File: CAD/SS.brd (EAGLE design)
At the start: 77 x 109 mm, 82 parts, among them Q1 SN74AHC-OR, Q2 UMD5N, Q4 SN74AHC-OR, Q5 BFP460, Q6 L78L05, Q7 NCP553, T1 MMBTRA104SS

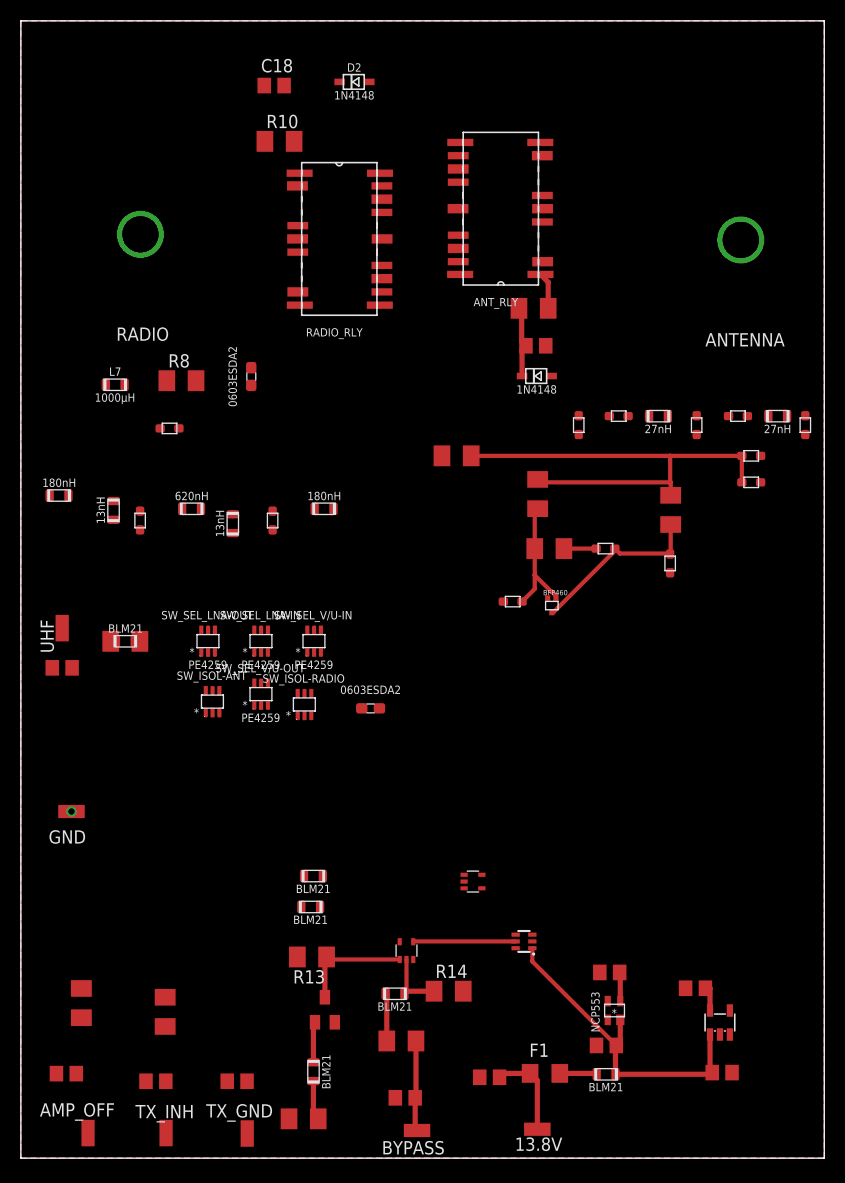
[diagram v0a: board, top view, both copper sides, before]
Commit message: Board: Pouring some copper over it
Started designing the board layout.
Plus, schematic: Fixed an error on 100R relay resistor placement
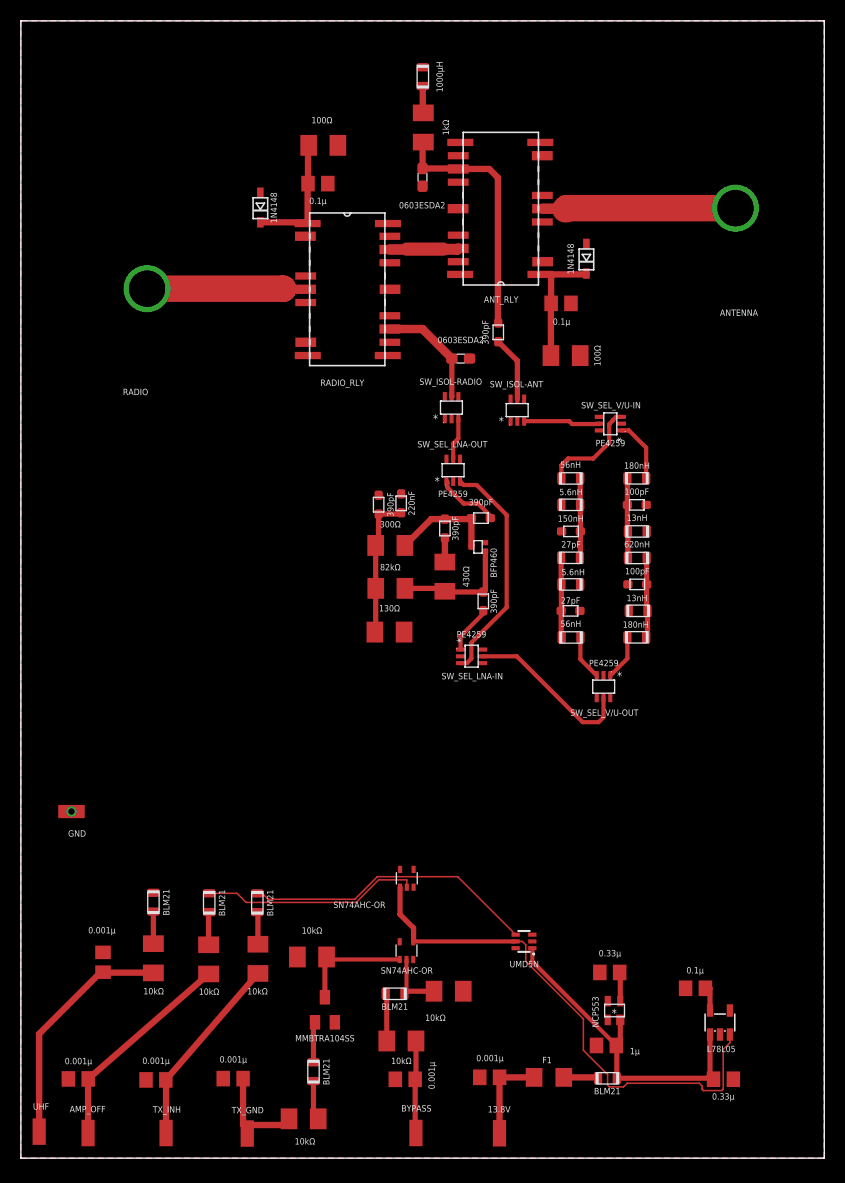
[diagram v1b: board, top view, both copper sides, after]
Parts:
- removed C3: 27pF, aarf:GRM18
- removed C4, C5: 6.8pF, aarf:GRM18
- added L10, L11: 5.6nH, aarf:0805
- added L9: 56nH, aarf:0805
- C6: value 43pF -> 27pF
- C7: value 4.7pF -> 27pF
- L6: value 27nH -> 56nH
- L8: value 27nH -> 150nH
- moved L5 57.0 mm to (59.0, 49.9)
- moved L4 51.2 mm to (59.2, 52.5), turned to 180 degrees
- moved UHF 48.3 mm to (1.75, 2.54), turned to 180 degrees
- moved C2 48.0 mm to (59.1, 55.0), turned to 0 degrees
- moved L3 43.0 mm to (59.1, 57.5), turned to 0 degrees
- moved L7 41.7 mm to (38.5, 103.7), turned to 90 degrees
- moved SW_ISOL-ANT 40.4 mm to (47.6, 71.7)
- moved L2 38.8 mm to (59.1, 60.1), turned to 0 degrees
- moved C10 35.8 mm to (34.3, 62.6), turned to 90 degrees
- moved SW_SEL_V/U-IN 35.3 mm to (56.5, 70.4), turned to 90 degrees
- moved C1 34.9 mm to (59.0, 62.6), turned to 180 degrees
- moved D4 34.6 mm to (42.2, 76.6)
- moved C11 33.9 mm to (36.4, 62.8), turned to 90 degrees
- moved R8 33.6 mm to (38.6, 98.8), turned to 270 degrees
- moved SW_SEL_V/U-OUT 32.9 mm to (55.9, 45.2), turned to 180 degrees
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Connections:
- removed net N$19: C5.P$1, C6.P$2, L8.P$2
- removed net N$20: C5.P$2, L6.P$1
- removed net N$30: R10.2, RL2.1
- new net N$11: C7.P$2, L11.P$1, L6.P$1, L8.P$2
- new net N$8: C6.P$2, L10.P$1, L8.P$1, L9.P$2
- net GND: now also L10.P$2, L11.P$2; no longer C3.P$1
- net N$1: now also C17.2, D2.C
- net N$18: now also C18.1, D3.C, R10.1, RL2.1; no longer C4.P$2, L8.P$1
- net N$21: no longer C7.P$2
- net N$4: now also L9.P$1; no longer C3.P$2, C4.P$1
- net RELAY_PWR: now also R10.2; no longer C17.2, C18.1, D2.C, D3.C, R10.1
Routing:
- net RLY_BYPASS: track 9.82 -> 50.7 mm
- net N$24: track 45.2 -> 13.7 mm
- net TO_BPF: track 0.00 -> 24.1 mm
- net N$12: track 0.00 -> 22.8 mm
- net LNA_BYPASS: track 0.00 -> 22.2 mm
- net AMP_OFF: track 0.00 -> 20.9 mm
- net N$15: track 0.00 -> 20.5 mm
- net RELAY_PWR: track 7.73 -> 28.2 mm
- net ANTENNA: track 0.00 -> 18.7 mm
- net N$26: track 0.00 -> 18.6 mm
- net BPF_OUT: track 0.00 -> 16.3 mm
- net RADIO: track 0.00 -> 13.1 mm
- net N$18: track 0.00 -> 12.1 mm
- net AMP+BPF_OUT: track 0.00 -> 10.8 mm
- net N$4: track 0.00 -> 9.98 mm
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
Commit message: More copper poured
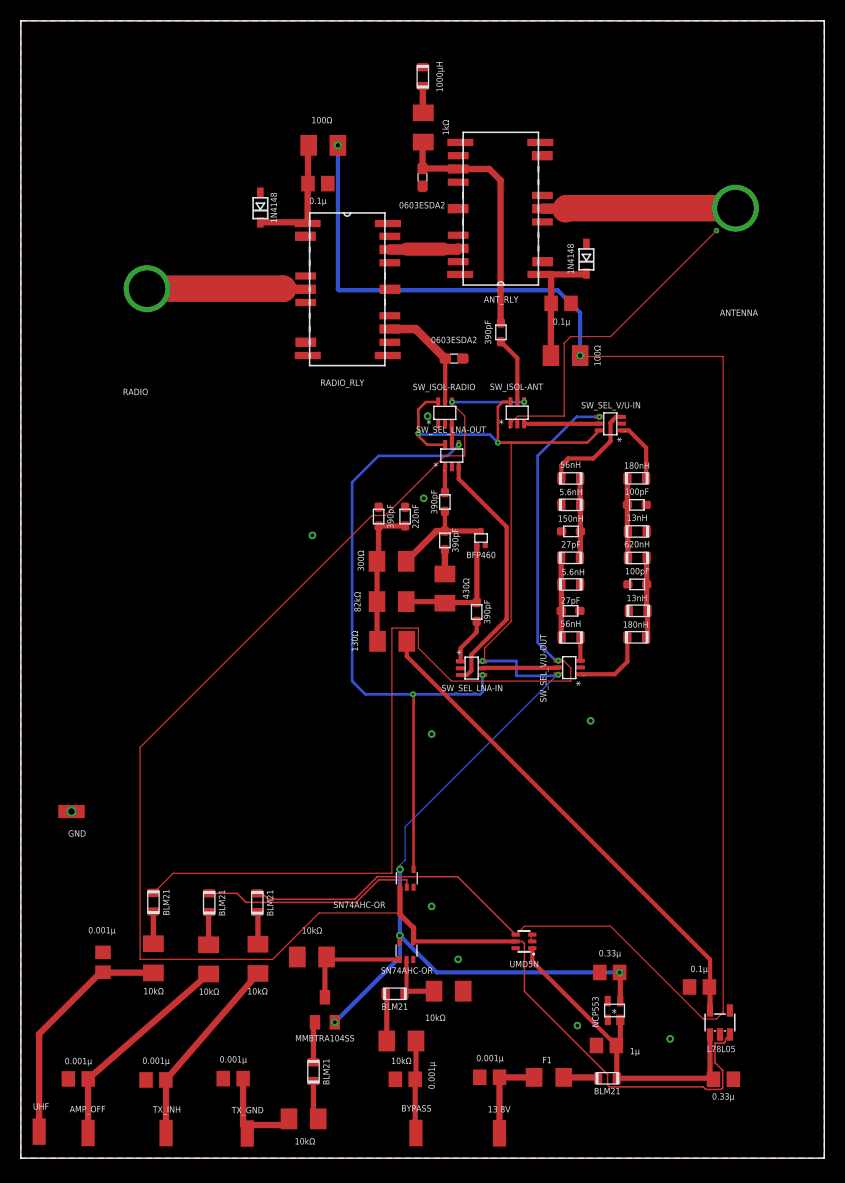
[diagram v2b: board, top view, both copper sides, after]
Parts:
- moved C12 3.78 mm to (40.6, 62.9), turned to 90 degrees
- moved SW_SEL_V/U-OUT 3.74 mm to (52.6, 47.0), turned to 90 degrees
- moved R3 1.53 mm to (35.5, 57.2)
- moved SW_SEL_LNA-OUT 1.40 mm to (41.3, 67.3)
- moved C11 1.33 mm to (36.8, 61.5)
- moved R1 1.28 mm to (35.5, 53.3)
- moved C8 1.20 mm to (43.7, 52.3)
- moved C10 1.14 mm to (34.3, 61.5)
- moved C9 1.14 mm to (40.6, 59.2)
- moved SW_SEL_LNA-IN 1.14 mm to (43.2, 47.0)
- moved R2 1.14 mm to (40.6, 54.6)
- moved R4 0.92 mm to (35.6, 49.5)
- moved Q5 0.90 mm to (44.1, 59.4), turned to 0 degrees
- moved SW_ISOL-RADIO 0.81 mm to (40.6, 71.4)
- moved D4 0.63 mm to (41.5, 76.6)
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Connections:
- net N$21 renamed UHF-OUT
- net N$3 renamed VHF-IN
- net N$4 renamed UHF-IN
- net N$7 renamed VHF-OUT
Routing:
- net RELAY_PWR: track 28.2 -> 171.0 mm, vias 0 -> 2
- net 3V: track 2.77 -> 130.0 mm, vias 0 -> 8
- net RLY_BYPASS: track 50.7 -> 153.8 mm, vias 0 -> 2
- net SEL_BPF_UHF: track 0.00 -> 99.0 mm, vias 0 -> 2
- net LNA_OFF: track 0.00 -> 62.7 mm, vias 0 -> 3
- net 5V: track 2.57 -> 47.5 mm
- net GND: track 0.00 -> 31.5 mm, vias 1 -> 11
- net BPF_OUT: track 16.3 -> 7.30 mm
- net LNA_OUT: track 6.09 -> 2.50 mm
- net VHF-OUT: track 4.34 -> 7.34 mm
- net RADIO: track 13.1 -> 15.2 mm
- net LNA-SW_OUT: track 4.10 -> 2.00 mm
- net UHF-OUT: track 4.31 -> 2.24 mm
- net LNA_BYPASS: track 22.2 -> 24.1 mm
- net N$36: track 0.00 -> 1.07 mm
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
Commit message: Progress
- Replaced capacitors and resistors with ones who has a PCB marking
- Poured more copper
- Added annotations
- Some block relocations
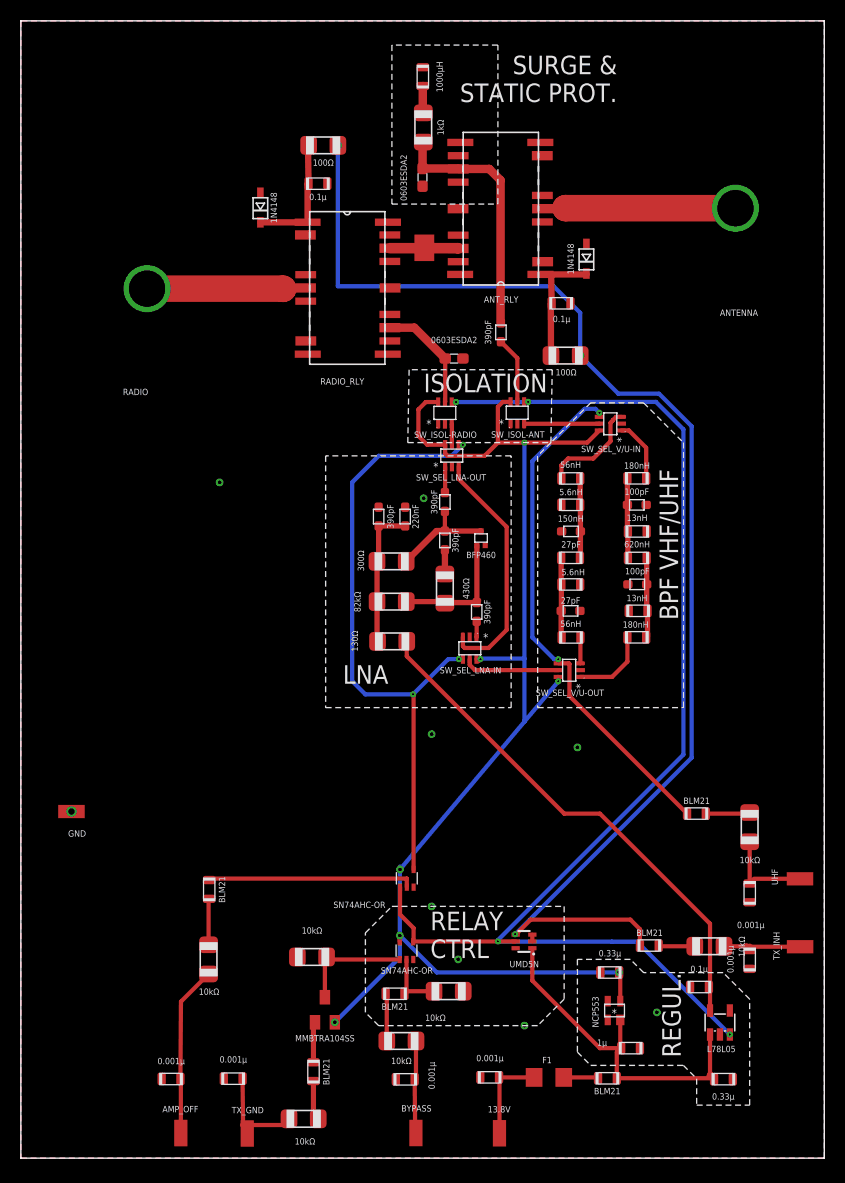
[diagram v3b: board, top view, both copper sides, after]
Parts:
- C13, C14, C15, C16, C17, C18, C19, C20, C21, C22, C23, C24: device rcl:C0805 -> aarf:0805
- R1, R10, R11, R12, R13, R14, R2, R3, R4, R5, R6, R7, R8, R9: device rcl:M1206 -> aarf:1206
- moved UHF 76.8 mm to (74.7, 26.8), turned to 270 degrees
- moved TX_INH 63.3 mm to (74.7, 20.3), turned to 270 degrees
- moved C19 62.3 mm to (69.8, 25.4), turned to 90 degrees
- moved R11 58.5 mm to (69.8, 31.7)
- moved C14 58.1 mm to (69.8, 19.0), turned to 90 degrees
- moved FB5 52.7 mm to (64.7, 33.0), turned to 180 degrees
- moved R5 43.3 mm to (66.0, 20.3), turned to 0 degrees
- moved FB2 37.8 mm to (60.2, 20.4), turned to 180 degrees
- moved AMP_OFF 8.89 mm to (15.3, 2.40)
- moved C20 8.89 mm to (14.4, 7.59)
- moved C23 2.33 mm to (58.4, 10.5), turned to 180 degrees
- moved SW_SEL_LNA-IN 1.93 mm to (43.0, 48.9), turned to 180 degrees
- moved FB6 1.27 mm to (18.0, 25.8)
- moved SW_SEL_V/U-OUT 0.25 mm to (52.6, 46.8)
- moved RL2 0.13 mm to (31.3, 83.4)
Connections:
- net N$6 renamed IN_DECPL
- net 0: now also C13.P$1; no longer C13.1
- net 13.8V: now also C21.P$2, C23.P$2; no longer C21.2, C23.2
- net 3V: now also C24.P$2; no longer C24.2
- net 5V: now also C22.P$2; no longer C22.2
- net GND: now also C14.P$1, C15.P$1, C16.P$1, C17.P$1, C18.P$2, C19.P$1, C20.P$1, C21.P$1, C22.P$1, C23.P$1, C24.P$1; no longer C14.1, C15.1, C16.1, C17.1, C18.2, C19.1, C20.1, C21.1, C22.1, C23.1, C24.1
- net N$1: now also C17.P$2; no longer C17.2
- net N$10: now also C16.P$2; no longer C16.2
- net N$12: now also C19.P$2; no longer C19.2
- net N$15: now also C20.P$2; no longer C20.2
- net N$16: now also C15.P$2; no longer C15.2
- net N$18: now also C18.P$1; no longer C18.1
- net N$26: now also C14.P$2; no longer C14.2
- net N$9: now also C13.P$2; no longer C13.2
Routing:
- net SEL_BPF_UHF: track 99.0 -> 49.5 mm
- net RELAY_PWR: track 171.0 -> 126.2 mm, vias 2 -> 3
- net RLY_BYPASS: track 153.8 -> 121.4 mm, vias 2 -> 4
- net GND: track 31.5 -> 0.13 mm, vias 11 -> 9
- net ANTENNA: track 18.7 -> 34.9 mm
- net N$12: track 23.1 -> 9.03 mm
- net N$26: track 18.6 -> 7.79 mm
- net N$15: track 20.5 -> 16.4 mm
- net N$19: track 3.56 -> 0.00 mm
- net LNA_IN: track 4.48 -> 1.53 mm
- net 5V: track 47.5 -> 49.5 mm
- net BPF_OUT: track 7.30 -> 9.26 mm
- net N$3: track 0.00 -> 1.91 mm
- net LNA_OFF: track 62.7 -> 60.9 mm
- net 13.8V: track 32.5 -> 34.2 mm
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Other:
- board text added: "BPF VHF/UHF"
- board text added: "ISOLATION"
- board text added: "LNA"
- board text added: "REGUL."
- board text added: "RELAY CTRL"
- board text added: "SURGE & STATIC PROT."

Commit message: More progress
- Featuring: CPWs (check https://resources.altium.com/p/pros-and-cons-of-different-high-frequency-transmission-line-types)
- Revamped BPF component layout
- Serious routing in RF side
- More labeled signals

Getting closer to the real deal
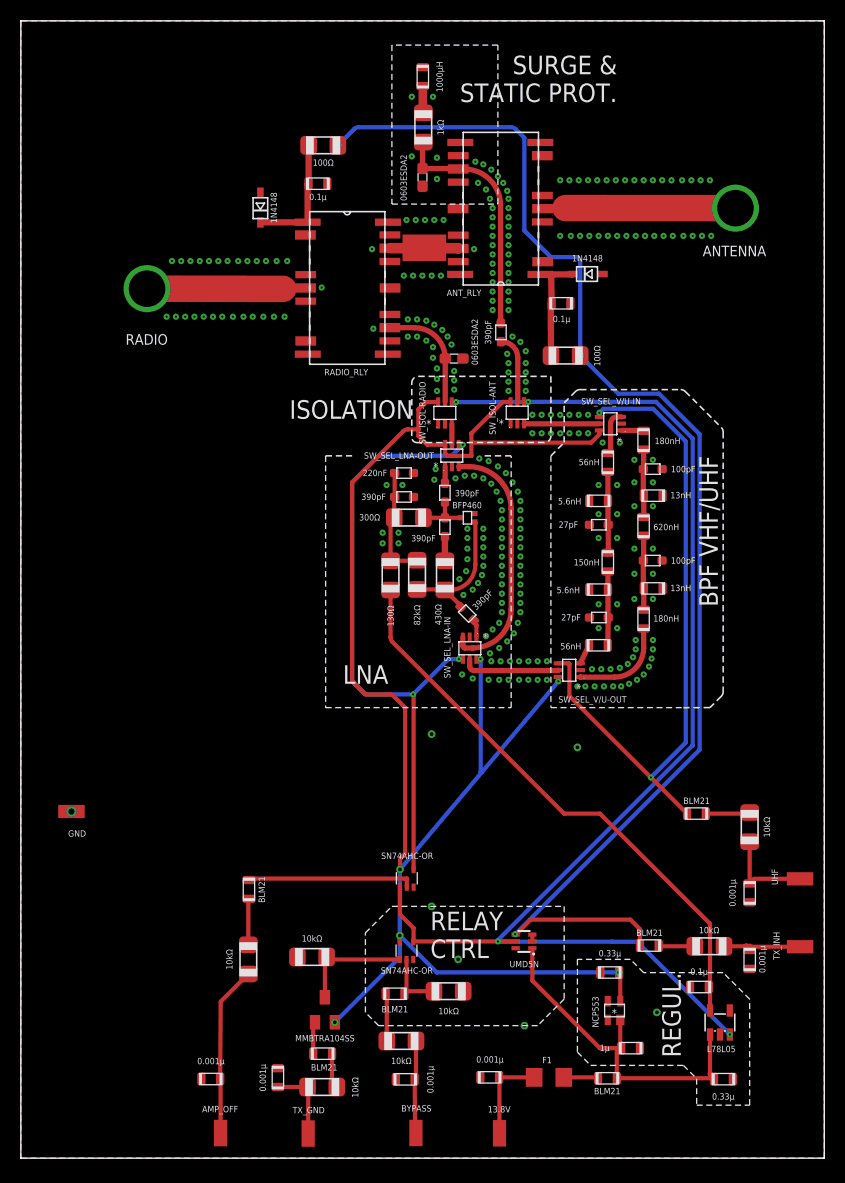
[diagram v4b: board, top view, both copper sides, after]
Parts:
- moved R4 6.33 mm to (35.4, 55.9), turned to 270 degrees
- moved TX_GND 5.84 mm to (27.5, 2.36)
- moved R3 4.50 mm to (37.2, 61.4)
- moved C15 4.30 mm to (24.6, 7.72), turned to 270 degrees
- moved C11 4.17 mm to (36.7, 65.7), turned to 0 degrees
- moved L9 3.87 mm to (56.3, 66.7), turned to 270 degrees
- moved AMP_OFF 3.81 mm to (19.1, 2.40)
- moved C20 3.81 mm to (18.2, 7.59)
- moved FB6 3.81 mm to (21.9, 25.8)
- moved R12 3.81 mm to (21.8, 19.1)
- moved C1 3.75 mm to (60.6, 66.0)
- moved L2 3.75 mm to (60.6, 63.5)
- moved L1 3.72 mm to (59.7, 68.8), turned to 270 degrees
- moved L8 3.60 mm to (56.3, 57.1), turned to 270 degrees
- moved R1 3.54 mm to (38.0, 55.9), turned to 90 degrees
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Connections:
- net N$1 renamed FEED-RA
- net N$18 renamed FEED-RB
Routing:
- net 3V: track 128.5 -> 159.1 mm, vias 7 -> 6
- net ANTENNA: track 34.9 -> 18.5 mm
- net SEL_BPF_UHF: track 49.5 -> 63.8 mm
- net UHF-IN: track 9.98 -> 4.24 mm
- net 5V: track 49.5 -> 55.1 mm
- net N$25: track 10.3 -> 5.09 mm
- net VHF-IN: track 6.00 -> 2.15 mm
- net AMP_OFF: track 19.8 -> 16.0 mm
- net N$16: track 10.2 -> 7.32 mm
- net N$24: track 13.7 -> 11.1 mm
- net N$3: track 1.91 -> 0.00 mm
- net VHF-OUT: track 7.45 -> 9.11 mm
- net RELAY_PWR: track 126.2 -> 127.8 mm
- net FEED-RA: track 13.3 -> 12.0 mm
- net TO_BPF: track 24.2 -> 22.8 mm
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
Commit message: Fixed crass error on LNA RF switch
it was flipped the ports RF1/RF2 (NO/NC)
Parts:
- VHF: value UHF -> VHF
- moved C8 3.76 mm to (39.2, 50.9), turned to 90 degrees
- moved C10 1.27 mm to (38.0, 63.4)
- moved C11 1.27 mm to (38.0, 65.7)
- moved Q5 1.27 mm to (44.1, 61.4)
- moved R1 1.27 mm to (39.2, 55.9)
- moved R3 1.27 mm to (38.5, 61.4)
- moved R4 1.27 mm to (36.7, 55.9)
- moved C12 1.27 mm to (41.9, 63.8)
- moved C9 1.27 mm to (41.9, 60.5)
- moved R2 1.27 mm to (41.9, 55.9)
- renumbered UHF to VHF
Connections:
- net SEL_BPF_UHF renamed SEL_BPF_VHF
- removed net LNA_BYPASS: SW_SEL_LNA-IN.3, SW_SEL_LNA-OUT.3
- removed net LNA_IN: C8.P$1, SW_SEL_LNA-IN.1
- removed net LNA_OUT: C12.P$2, SW_SEL_LNA-OUT.1
- new net LNA-BYPASS: SW_SEL_LNA-IN.1, SW_SEL_LNA-OUT.1
- new net N$1: C12.P$2, SW_SEL_LNA-OUT.3
- new net N$4: C8.P$1, SW_SEL_LNA-IN.3
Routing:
- net LNA-BYPASS: track 0.00 -> 25.5 mm
- net LNA_BYPASS: track 23.4 -> 0.00 mm
- net LNA_OFF: track 60.9 -> 55.9 mm
- net N$4: track 0.00 -> 3.15 mm
- net 5V: track 55.1 -> 56.8 mm
- net LNA_IN: track 1.70 -> 0.00 mm
- net N$1: track 0.00 -> 1.62 mm
- net LNA_OUT: track 1.61 -> 0.00 mm
- net 3V: track 159.1 -> 158.1 mm, vias 6 -> 8
- net GND: vias 294 -> 296
